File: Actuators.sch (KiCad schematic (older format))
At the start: 14 parts, among them J1 SERVO DCDC 5V, J10 Servo, J3 Actuator1, J4 Actuator2, J9 Servo, U6 DRV8847_TSSOP

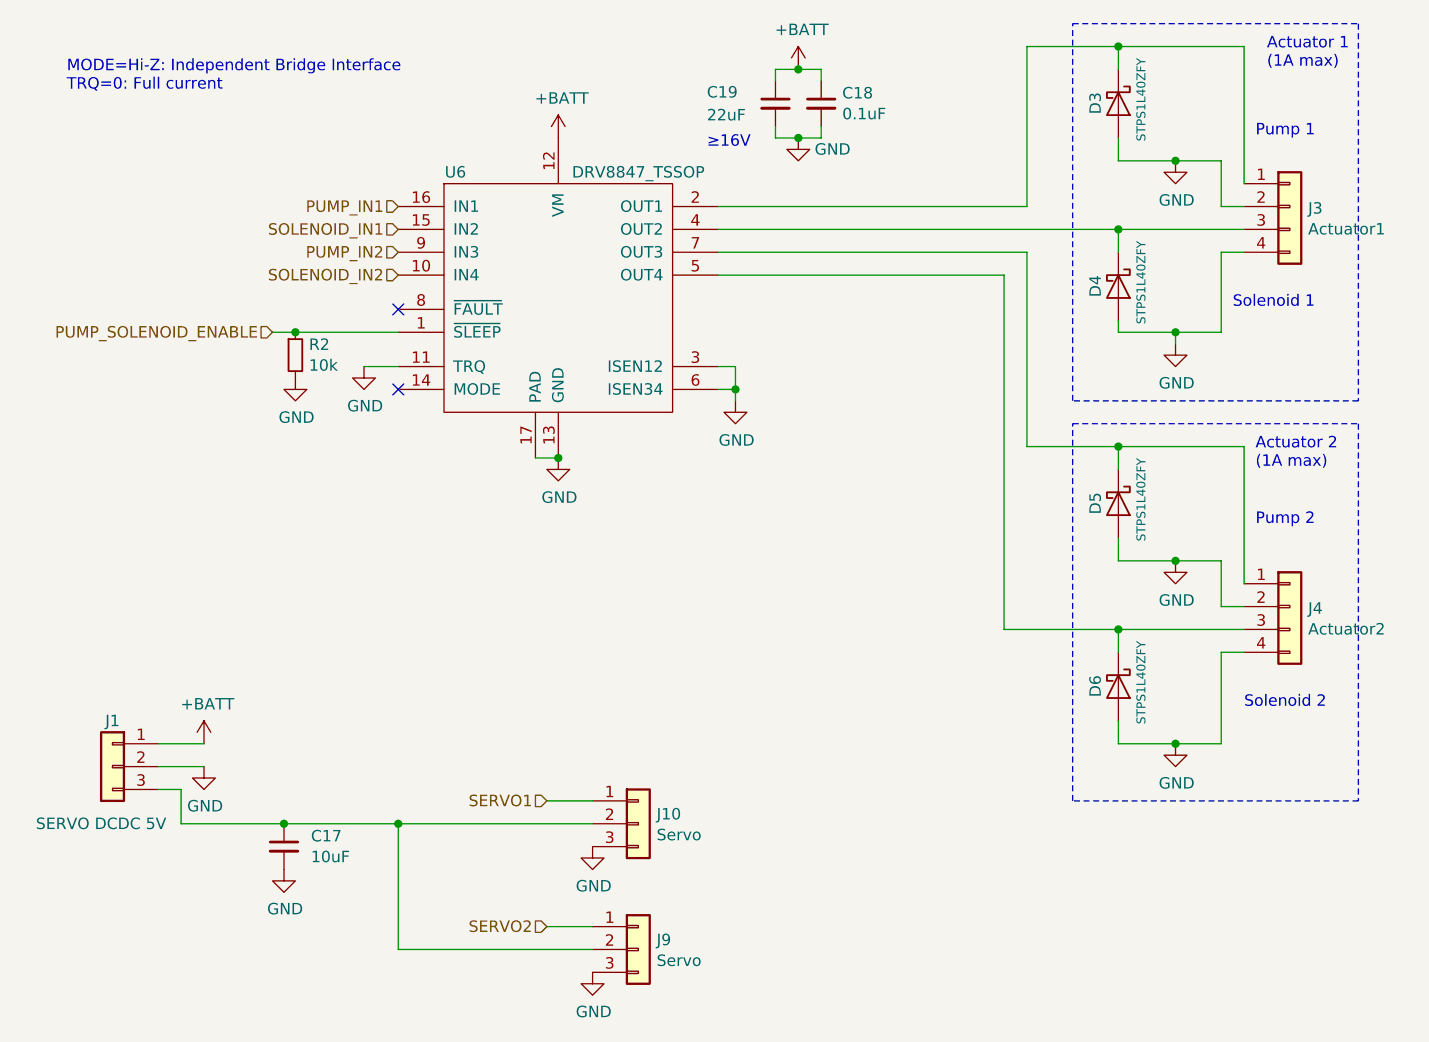
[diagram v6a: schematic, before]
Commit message: Update DigiKey references
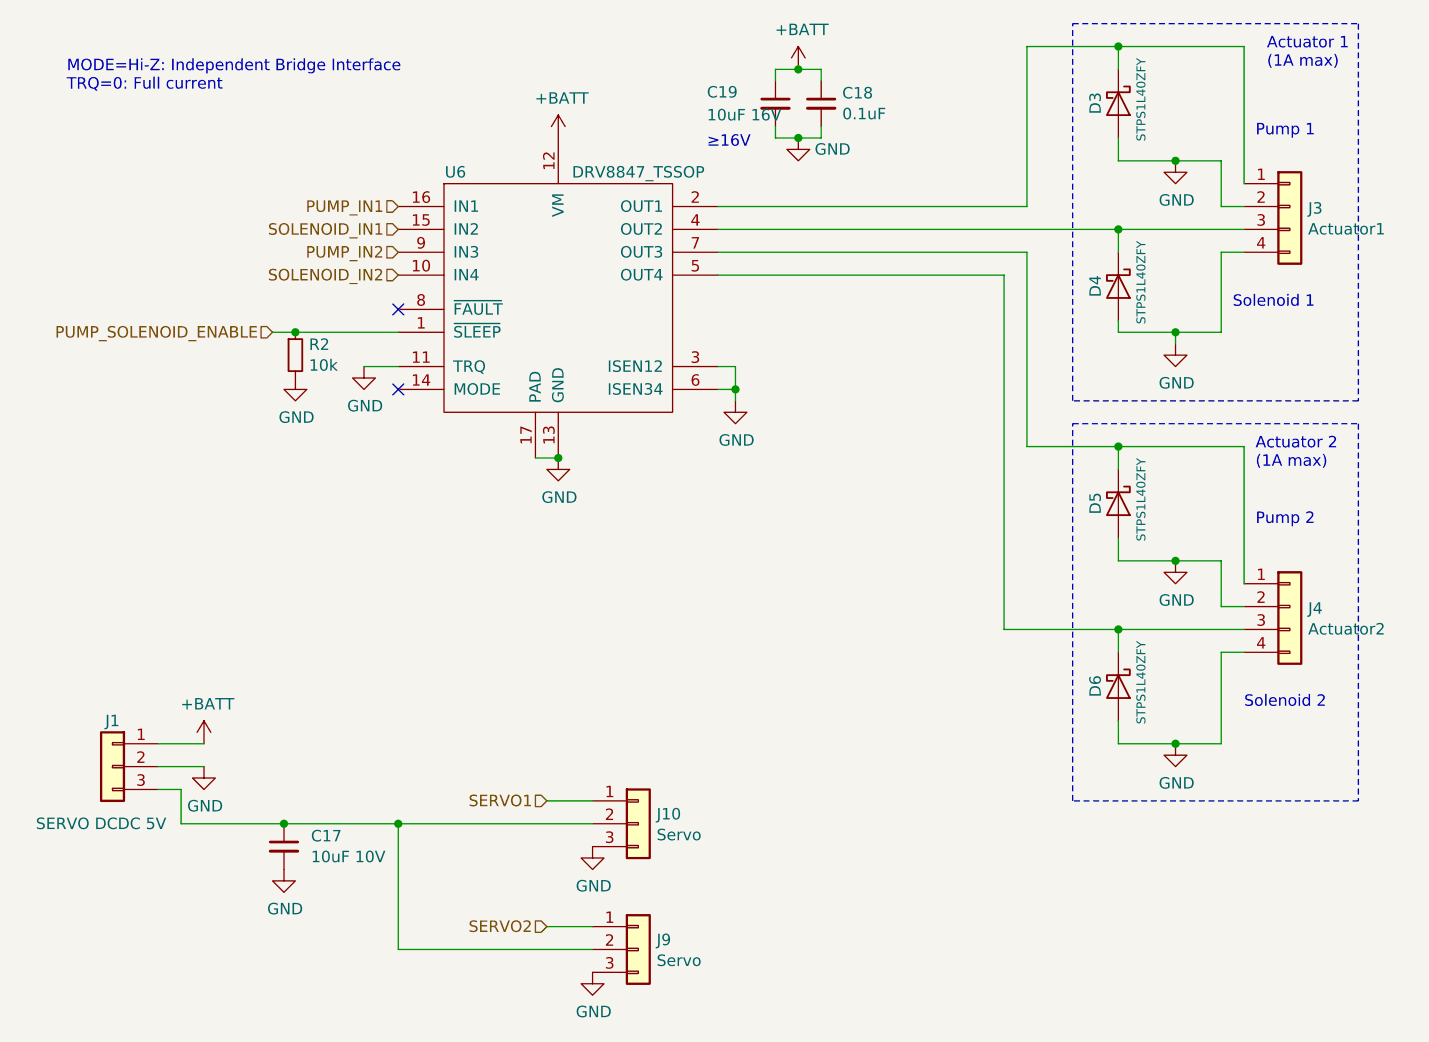
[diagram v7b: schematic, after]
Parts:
- C17: value 10uF -> 10uF 10V; digikey# 399-7442-1-ND -> 399-8155-1-ND
- C19: value 22uF -> 10uF 16V; digikey# PCE4240CT-ND -> 399-7442-1-ND
- U6: digikey# (none) -> 296-53424-1-ND
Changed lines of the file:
@@
 AR Path="/5E1FB153/5E3A79F5" Ref="C17"  Part="1"
 F 0 "C17" H 3468 5496 50  0000 L CNN
-F 1 "10uF" H 3468 5405 50  0000 L CNN
+F 1 "10uF 10V" H 3468 5405 50  0000 L CNN
 F 2 "Capacitor_SMD:C_1206_3216Metric" H 3388 5300 50  0001 C CNN
 F 3 "~" H 3350 5450 50  0001 C CNN
-F 4 "399-7442-1-ND" H 3350 5450 50  0001 C CNN "digikey#"
+F 4 "399-8155-1-ND" H 3350 5450 50  0001 C CNN "digikey#"
 	1    3350 5450
 	1    0    0    -1
@@
 F 2 "Package_SO:TSSOP-16-1EP_4.4x5mm_P0.65mm" H 4550 3000 50  0001 C CNN
 F 3 "http://www.ti.com/lit/ds/symlink/drv8847.pdf" H 4550 3000 50  0001 C CNN
-F 4 "" H 4550 3050 50  0001 C CNN "digikey#"
+F 4 "296-53424-1-ND" H 4550 3050 50  0001 C CNN "digikey#"
 	1    4550 3050
 	1    0    0    -1
@@
 AR Path="/5E1FB153/5E4761AC" Ref="C19"  Part="1"
 F 0 "C19" H 5200 2250 50  0000 L CNN
-F 1 "22uF" H 5200 2150 50  0000 L CNN
+F 1 "10uF 16V" H 5200 2150 50  0000 L CNN
 F 2 "Capacitor_SMD:C_1206_3216Metric" H 5538 2050 50  0001 C CNN
 F 3 "~" H 5500 2200 50  0001 C CNN
-F 4 "PCE4240CT-ND" H 5500 2200 50  0001 C CNN "digikey#"
+F 4 "399-7442-1-ND" H 5500 2200 50  0001 C CNN "digikey#"
 	1    5500 2200
 	1    0    0    -1
